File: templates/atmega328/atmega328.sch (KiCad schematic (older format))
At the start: 0 parts

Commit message: Finished Atmega328 template, including board layout.
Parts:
- added C1, C5, C7, C8, C9: 100nF, Wickerlib:0603, symbol CAP-CER-0.1UF-100V-X7R-0603
- added C2, C6: 10uF 25V, Wickerlib:1210, symbol CAP-CER-10UF-25V-X7R-1210
- added C3, C4: 22pF, Wickerlib:0603, symbol CAP-CER-22PF-100V-C0G-NP0-0603
- added D1: 14V, Wickerlib:Diode_SMA, symbol DIODE-TVS-SMAJ14A-13-F-SMA
- added D2, D3: 20V 1A, Wickerlib:Diode_SMA, symbol DIODE-SCHOTTKY-20V-1A-SS12-SMA
- added F1: 1.1A 25V, Wickerlib:1812, symbol FUSE-RESET-1.1A-25V-MF-MSMF
- added J1: INPUT, Wickerlib:OSTVN02A150, symbol CONN-TERM-SCREW-GREEN-2.54MM-2POS-TH
- added J2: FTDI, Wickerlib:Pin_Header_Straight_1x06, symbol HEADER-MALE-6POS-TH-1x06-P0.1IN
- added J3: ISP-2560, Wickerlib:Pin_Header_Straight_2x03, symbol HEADER-MALE-6POS-TH-2x3-P0.1IN
- added J4: DIGOUT1, Wickerlib:Pin_Header_Straight_1x10, symbol HEADER-FEMALE-10POS-TH-1x10-P0.1IN
- added J5: DIGOUT2, Wickerlib:Pin_Header_Straight_1x10, symbol HEADER-FEMALE-10POS-TH-1x10-P0.1IN
- added LED1: AMBER, Wickerlib:0603, symbol LED-AMBER-0603-SMT-L296-Q2R2
- added R1: 10K, Wickerlib:0805, symbol RES-10K-5%-1/8W-0805
- added R2: 1K, Wickerlib:0603, symbol RES-1K-1%-1/10W-0603
- added S1: RESET, Wickerlib:SW-B3U-1000P, symbol SWITCH-TACTILE-SPST-NO-0.05A-12V
- added U1: NCP1117-5V, Wickerlib:DPAK, symbol IC-REG-LDO-5V-1.1A-NCP1117-5V-DPAK
- added U2: ATMEGA328, Wickerlib:TQFP-32_7x7mm_Pitch0.8mm, symbol IC-MCU-ATMEGA328-TQFP32
- added X1: 16MHz 18pF, Wickerlib:CRYSTAL-CTS-4SMD, symbol CRYSTAL-16MHZ-18PF-40OHM-CTS-4SMD
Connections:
- new net: C3.1, U2.7 ((PCINT6/XTAL1/TOSC1)PB6), X1.1 (EN)
- new net: C4.1, U2.8 ((PCINT7/XTAL2/TOSC2)PB7), X1.3 (OUT)
- new net: C6.1, D3.2 (A), U1.2 (OUT)
- new net: D2.1 (K), F1.2
- new net: LED1.2 (A), R2.2
- new net +12V: C2.1, F1.1, U1.3 (IN)
- new net +5V: C5.1, C7.1, C8.1, C9.1, D3.1 (K), J2.4 (P4), J3.2 (P2), R1.1, U2.18 (AVCC), U2.20 (AREF), U2.4 (VCC), U2.6 (VCC)
- new net A0: J5.3 (P3), U2.23 ((PCINT8/ADC0)PC0)
- new net A1: J5.4 (P4), U2.24 ((PCINT9/ADC1)PC1)
- new net A2: J5.5 (P5), U2.25 ((PCINT10/ADC2)PC2)
- new net A3: J5.6 (P6), U2.26 ((PCINT11/ADC3)PC3)
- new net A4: J5.7 (P7), U2.27 ((PCINT12/SDA/ADC4)PC4)
- new net A5: J5.8 (P8), U2.28 ((PCINT13/SCL/ADC5)PC5)
- new net A6(*): J5.9 (P9), U2.19 (ADC6)
- new net A7(*): J5.10 (P10), U2.22 (ADC7)
- new net D0: J2.2 (P2), U2.30 ((PCINT16/RXD)PD0)
- new net D1: J2.3 (P3), U2.31 ((PCINT17/TXD)PD1)
- new net D10: J4.9 (P9), U2.14 ((PCINT2/OC1B/~SS~)PB2)
- new net D11: J3.1 (P1), J4.10 (P10), U2.16 ((PCINT4/MISO)PB4)
- new net D12: J3.4 (P4), J5.1 (P1), U2.15 ((PCINT3/OC2A/MOSI)PB3)
- new net D13: J3.3 (P3), J5.2 (P2), U2.17 ((PCINT5/SCK)PB5)
- new net D2: J4.1 (P1), U2.32 ((PCINT18/INT0)PD2)
- new net D3: J4.2 (P2), U2.1 ((PCINT19/OC2B/INT1)PD3)
- new net D4: J4.3 (P3), U2.2 ((PCINT20/XCK/T0)PD4)
- new net D5: J4.4 (P4), U2.9 ((PCINT21/OC0B/T1)PD5)
- new net D6: J4.5 (P5), U2.10 ((PCINT22/OC0A/AIN0)PD6)
- new net D7: J4.6 (P6), R2.1, U2.11 ((PCINT23/AIN1)PD7)
- new net D8: J4.7 (P7), U2.12 ((PCINT0/CLKO/ICP1)PB0)
- new net D9: J4.8 (P8), U2.13 ((PCINT1/OC1A)PB1)
- new net FTDI_RESET: C1.2, J2.1 (P1)
- new net GND: C2.2, C3.2, C4.2, C5.2, C6.2, C7.2, C8.2, C9.2, D1.2, J1.2 (P2), J2.6 (P6), J3.6 (P6), LED1.1 (K), S1.1, U1.1 (GND), U2.21 (GND), U2.3 (GND), U2.5 (GND), X1.2 (GND), X1.4 (GND)
- new net VIN: D1.1, D2.2 (A), J1.1 (P1)
- new net ~RESET: C1.1, J3.5 (P5), R1.2, S1.2, U2.29 ((PCINT14/~RESET~)PC6)
- no-connect marks 0 -> 1
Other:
- note added: "* ADC6 and ADC7 can only\nbe used as analog inputs"
- note added: "Analog\nReference"
- note added: "Heartbeat"
- note added: "ICSP\nProgrammer"
- note added: "MAIN INPUT POWER\n-----------\nSCREW TERMINAL\n12V 1A RATING\n"
- note added: "To FTDI\nProgrammer"

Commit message: Removed implementation and left only the raw template.
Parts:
- C1, C3, C4, C5, C7, C8, C9, LED1, R2: footprint Wickerlib:0603 -> Wickerlib:RLC-0603-SMD
- C2, C6: footprint Wickerlib:1210 -> Wickerlib:RLC-1210-SMD
- D1, D2, D3: footprint Wickerlib:Diode_SMA -> Wickerlib:DIODE-SMA
- F1: footprint Wickerlib:1812 -> Wickerlib:RLC-1812-SMD
- J1: footprint Wickerlib:OSTVN02A150 -> Wickerlib:CONN-ONSHORE-SCREW-GREEN-2PIN-TH
- J2: footprint Wickerlib:Pin_Header_Straight_1x06 -> Wickerlib:CONN-HEADER-STRAIGHT-P2.54MM-1x06
- J3: footprint Wickerlib:Pin_Header_Straight_2x03 -> Wickerlib:CONN-HEADER-STRAIGHT-P2.54MM-2x03
- J4, J5: footprint Wickerlib:Pin_Header_Straight_1x10 -> Wickerlib:CONN-HEADER-STRAIGHT-P2.54MM-1x10
- R1: footprint Wickerlib:0805 -> Wickerlib:RLC-0805-SMD
- S1: footprint Wickerlib:SW-B3U-1000P -> Wickerlib:SWITCH-OMRON-MOMENTARY-SMD-B3U-1000P
- U2: footprint Wickerlib:TQFP-32_7x7mm_Pitch0.8mm -> Wickerlib:TQFP-32-7x7MM-P0.8MM

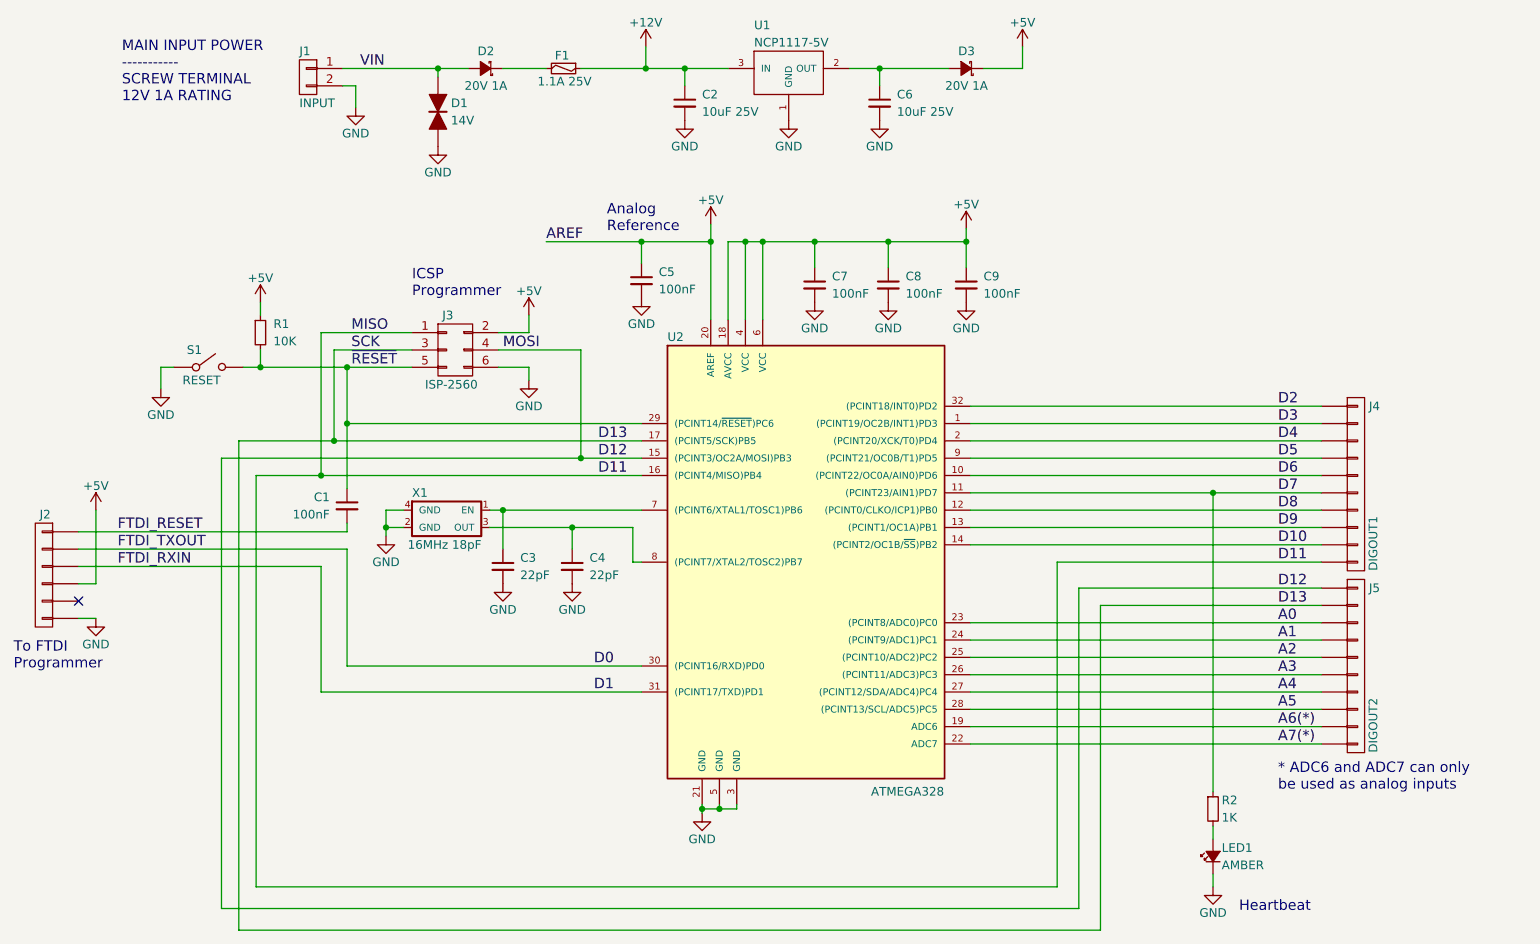
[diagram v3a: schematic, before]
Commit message: Created basic ATMEGA328 breakout board
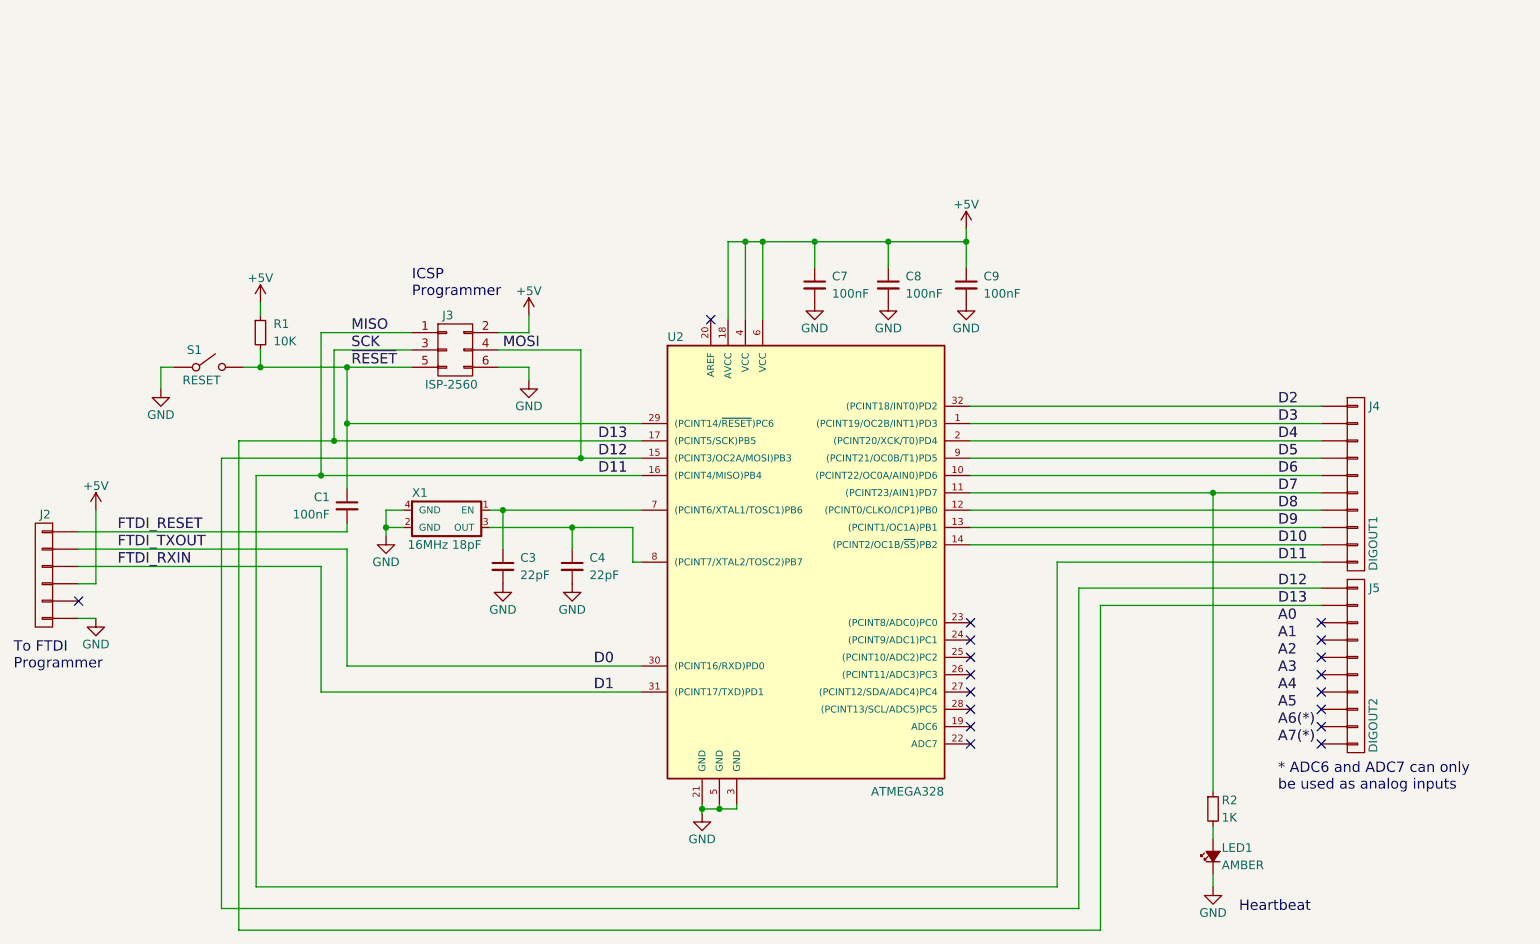
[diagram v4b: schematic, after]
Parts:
- removed C2, C6: 10uF 25V, Wickerlib:RLC-1210-SMD, symbol CAP-CER-10UF-25V-X7R-1210
- removed C5: 100nF, Wickerlib:RLC-0603-SMD, symbol CAP-CER-0.1UF-100V-X7R-0603
- removed D1: 14V, Wickerlib:DIODE-SMA, symbol DIODE-TVS-SMAJ14A-13-F-SMA
- removed D2, D3: 20V 1A, Wickerlib:DIODE-SMA, symbol DIODE-SCHOTTKY-20V-1A-SS12-SMA
- removed F1: 1.1A 25V, Wickerlib:RLC-1812-SMD, symbol FUSE-RESET-1.1A-25V-MF-MSMF
- removed J1: INPUT, Wickerlib:CONN-ONSHORE-SCREW-GREEN-2PIN-TH, symbol CONN-TERM-SCREW-GREEN-2.54MM-2POS-TH
- removed U1: NCP1117-5V, Wickerlib:DPAK, symbol IC-REG-LDO-5V-1.1A-NCP1117-5V-DPAK
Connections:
- net +5V: no longer U2.20 (AREF)
- net A0: no longer J5.3 (P3), U2.23 ((PCINT8/ADC0)PC0)
- net A1: no longer J5.4 (P4), U2.24 ((PCINT9/ADC1)PC1)
- net A2: no longer J5.5 (P5), U2.25 ((PCINT10/ADC2)PC2)
- net A3: no longer J5.6 (P6), U2.26 ((PCINT11/ADC3)PC3)
- net A4: no longer J5.7 (P7), U2.27 ((PCINT12/SDA/ADC4)PC4)
- net A5: no longer J5.8 (P8), U2.28 ((PCINT13/SCL/ADC5)PC5)
- net A6(*): no longer J5.9 (P9), U2.19 (ADC6)
- net A7(*): no longer J5.10 (P10), U2.22 (ADC7)
- no-connect marks 1 -> 18
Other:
- note removed: "Analog\nReference"
- note removed: "MAIN INPUT POWER\n-----------\nSCREW TERMINAL\n12V 1A RATING\n"
